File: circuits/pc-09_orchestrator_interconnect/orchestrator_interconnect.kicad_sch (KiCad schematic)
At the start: 14 parts, among them J4 Conn_01x08, J5 Conn_01x05, J6 Conn_01x07, U1 4078, U2 74HC74, U3 4011, U4 4081, U5 4081, U6 74HC138

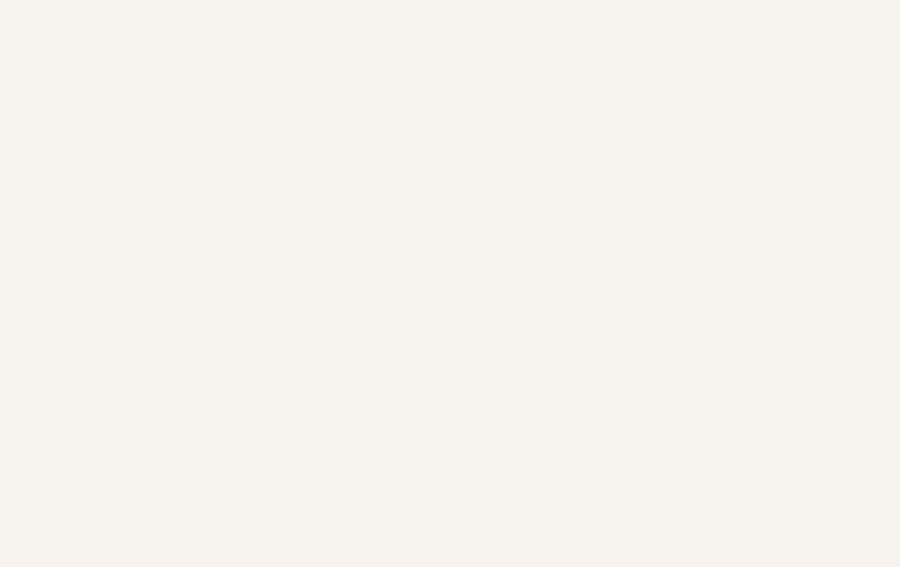
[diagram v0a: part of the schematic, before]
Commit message: add filter and decoupling capacitors to all boards
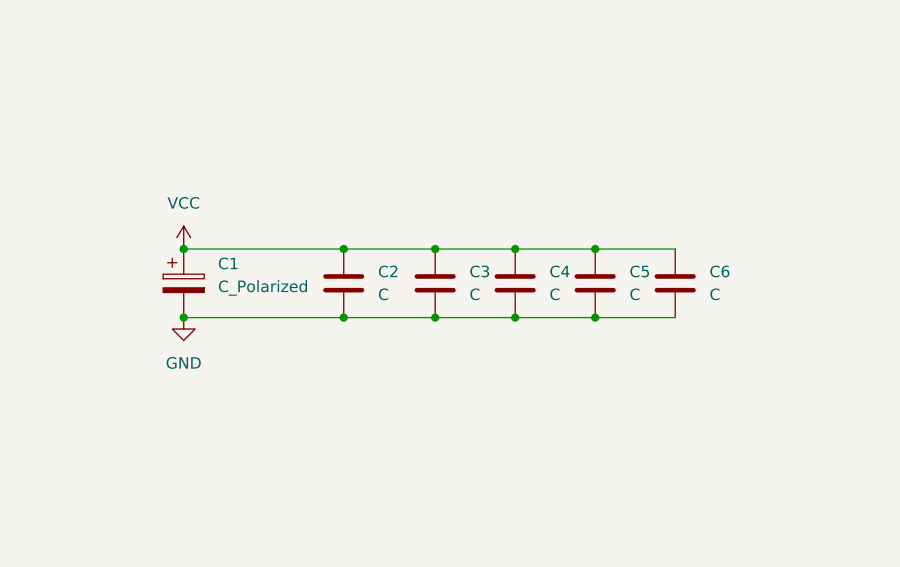
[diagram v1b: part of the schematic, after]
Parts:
- added C1: C_Polarized, Capacitor_SMD:CP_Elec_5x5.3, symbol Device:C_Polarized
- added C2, C3, C4, C5, C6: C, Capacitor_SMD:C_0603_1608Metric, symbol Device:C
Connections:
- net GND: now also C1.2, C2.2, C3.2, C4.2, C5.2, C6.2
- net VCC: now also C1.1, C2.1, C3.1, C4.1, C5.1, C6.1
